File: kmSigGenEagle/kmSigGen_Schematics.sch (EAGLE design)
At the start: 36 parts, among them IC1 MEGA8-P

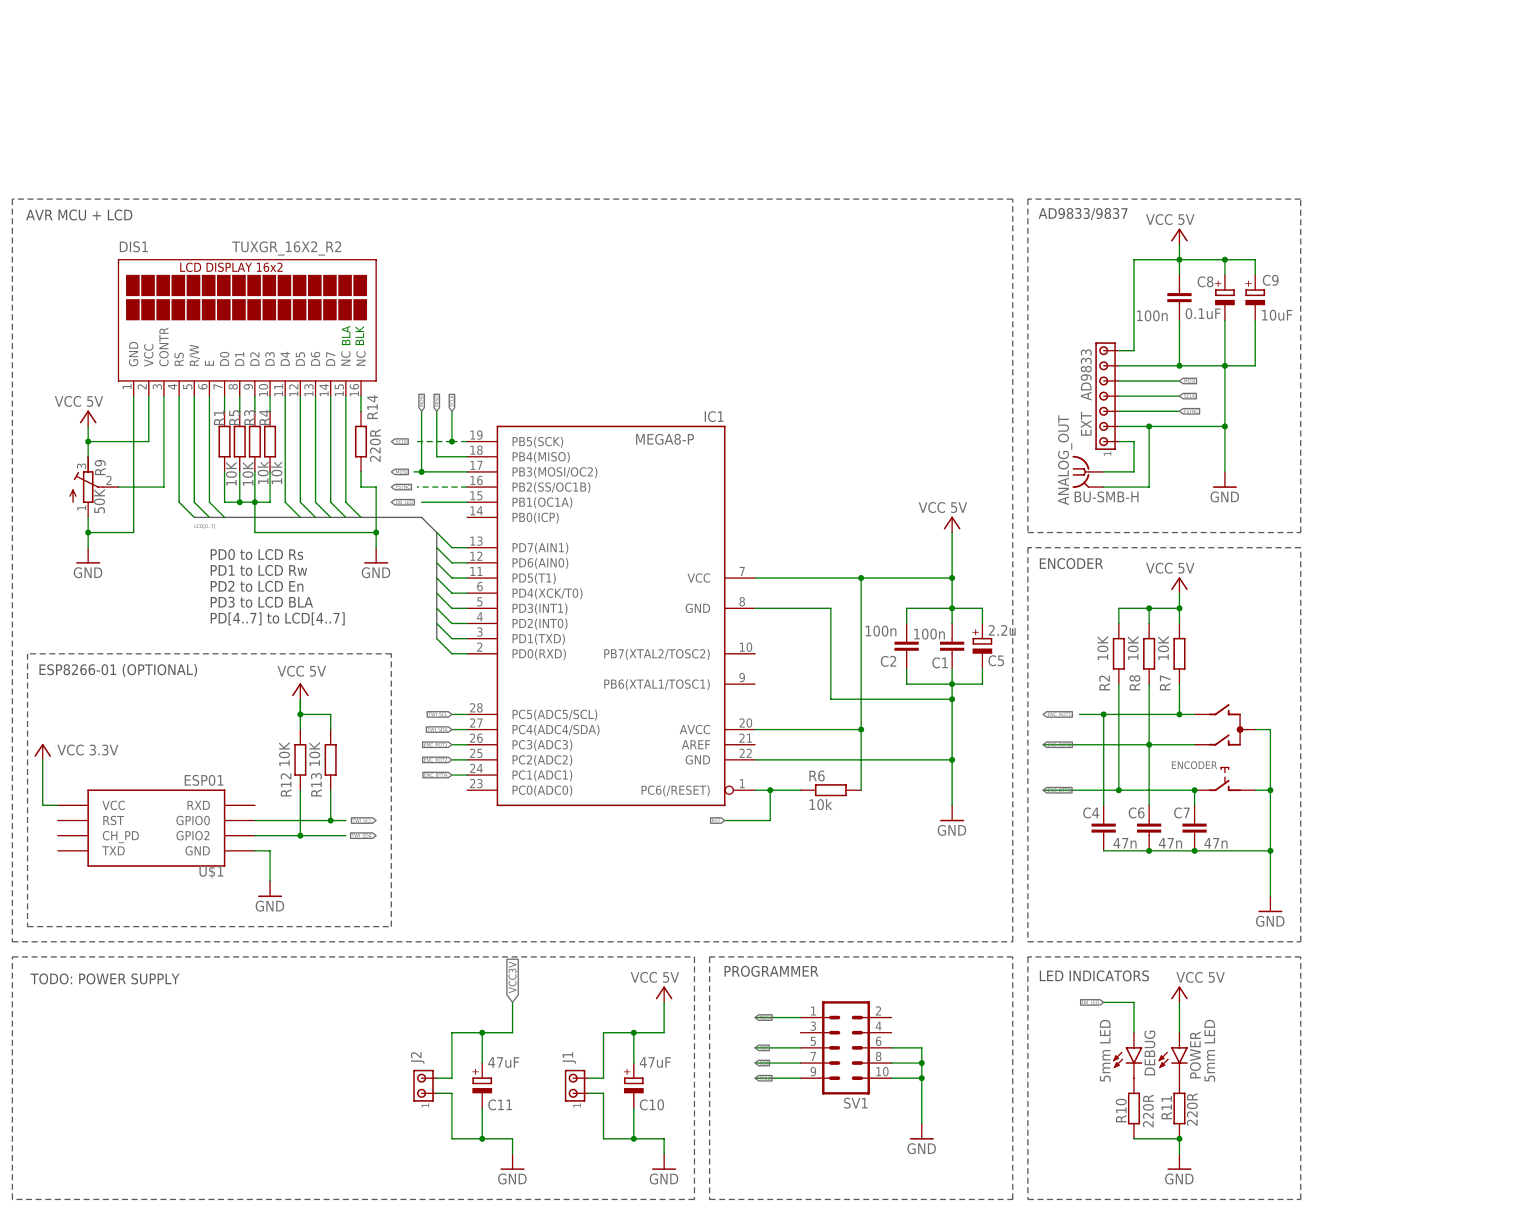
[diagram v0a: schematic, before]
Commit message: Updated schematics of encoder hardware
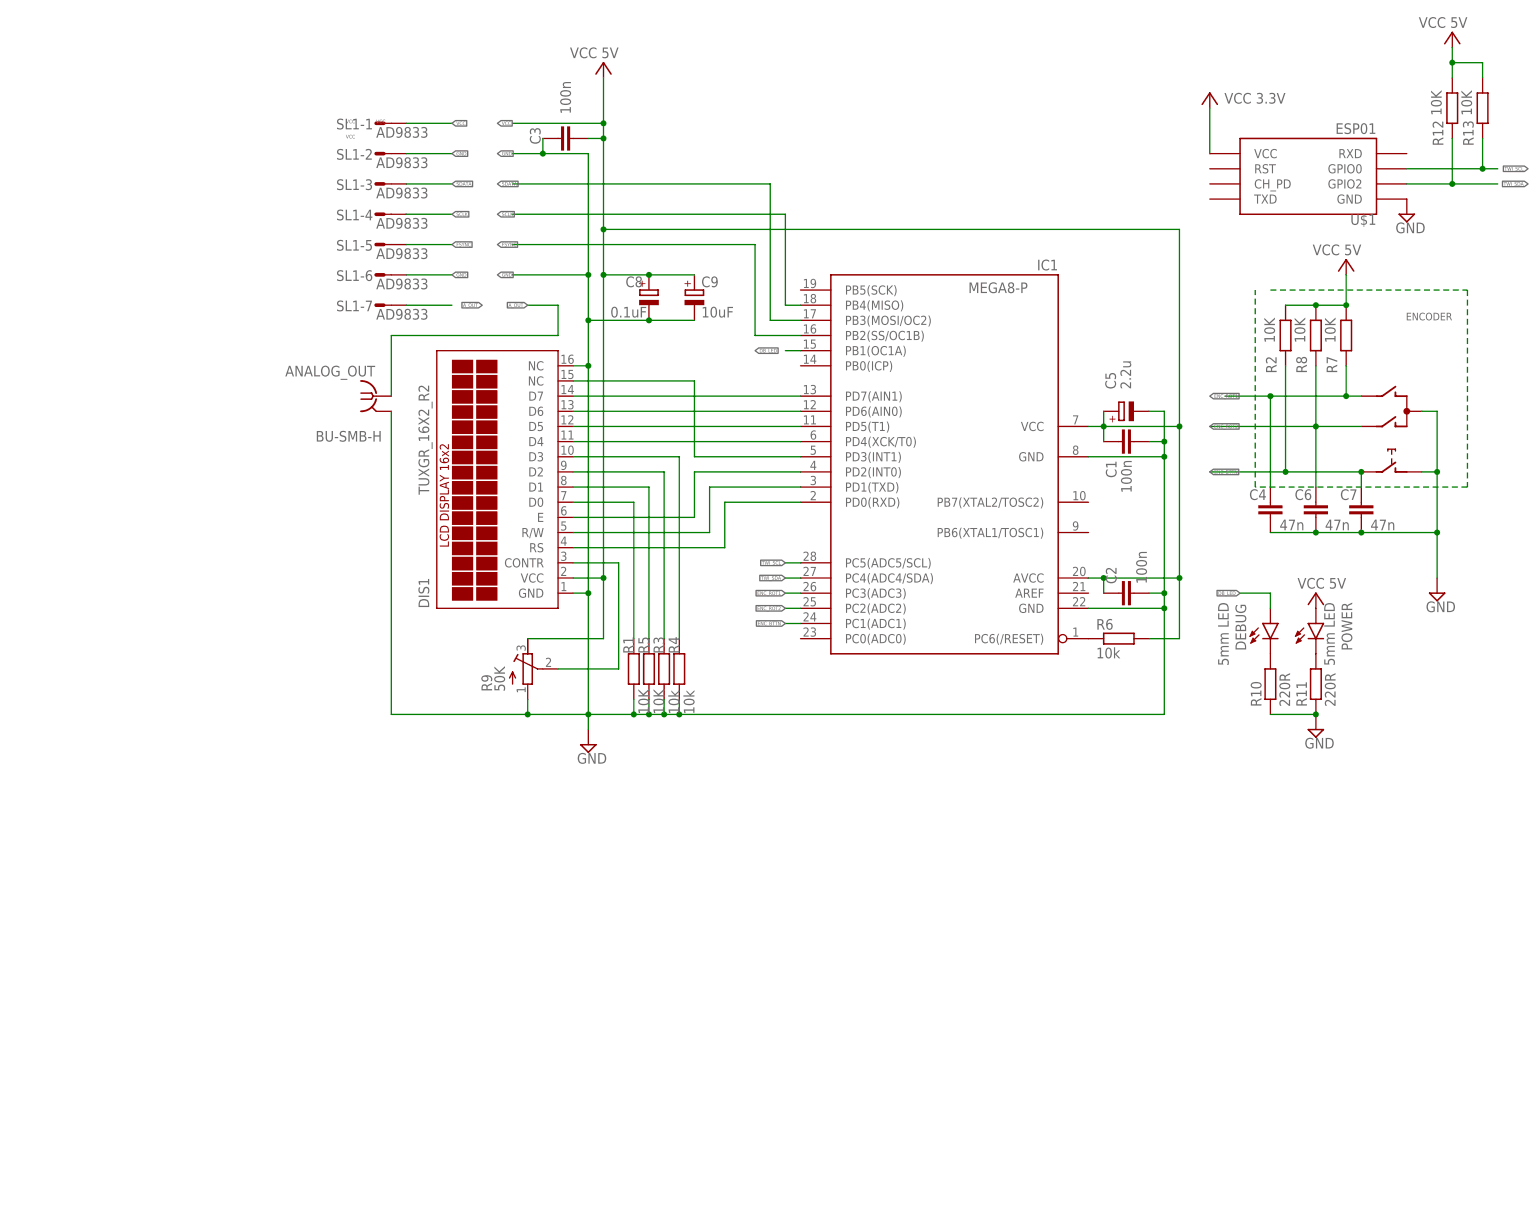
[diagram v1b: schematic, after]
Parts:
- removed C10, C11: 47uF, rcl:CPOL-EUB45181B
- removed EXT: AD9833, con-amp:MTA07-100
- removed J1, J2: (no value), con-amp:MTA02-156
- removed R14: 220R, rcl:R-EU_0207/10
- removed SV1: (no value), con-ml:ML10
- added SL1: AD9833, con-amp-quick:M07S
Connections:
- net LCD0 renamed N$7
- net LCD1 renamed N$8
- net LCD2 renamed N$9
- net LCD3 renamed N$6
- net LCD4 renamed N$5
- net LCD5 renamed N$4
- net LCD6 renamed N$3
- net LCD7 renamed LCD_D7
- removed net MISO: IC1.PB4(MISO), SV1.9
- removed net MOSI: EXT.5, IC1.PB3(MOSI/OC2), SV1.1
- removed net N$19: ANALOG_OUT.1, EXT.1
- removed net N$2: DIS1.NC@2, R14.2
- removed net RST: IC1.PC6(/RESET), R6.1, SV1.5
- removed net SCK: SV1.7
- removed net VCC3V: C11.+, J2.2, U$1.VCC
- new net A_OUT: ANALOG_OUT.1, SL1-7.S
- new net N$13: IC1.PC6(/RESET), R6.1
- new net SDATA: IC1.PB3(MOSI/OC2), SL1-3.S
- net FSYNC: now also SL1-5.S; no longer EXT.3
- net GND: now also C1.2, C2.2, DIS1.NC@2, SL1-2.S, SL1-6.S; no longer C1.1, C10.-, C11.-, C2.1, EXT.2, EXT.6, J1.1, J2.1, R14.1, SV1.10, SV1.6, SV1.8
- net SCLK: now also IC1.PB4(MISO), SL1-4.S; no longer EXT.4, IC1.PB5(SCK)
- net VCC: now also C1.1, C2.1, SL1-1.S, U$1.VCC; no longer C1.2, C10.+, C2.2, EXT.7, J1.2
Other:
- note removed: "AD9833/9837"
- note removed: "AVR MCU + LCD"
- note removed: "BLA"
- note removed: "BLK"
- note removed: "ENCODER"
- note removed: "ESP8266-01 (OPTIONAL)"
- note removed: "LED INDICATORS"
- note removed: "PD0 to LCD Rs PD1 to LCD Rw PD2 to LCD En PD3 to LCD BLA PD[4..7] to LCD[4..7]"
- note removed: "PROGRAMMER"
- note removed: "TODO: POWER SUPPLY"
- moved on the sheet: ANALOG_OUT, C1, C2, C4, C5, C6, C7, C8, C9, DEBUG, DIS1, ENCODER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

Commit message: Fixed issue with clearing wavetype after updating frequency from WiFi module; cleanup of Eagle Schematics, version changed to 1.0.1
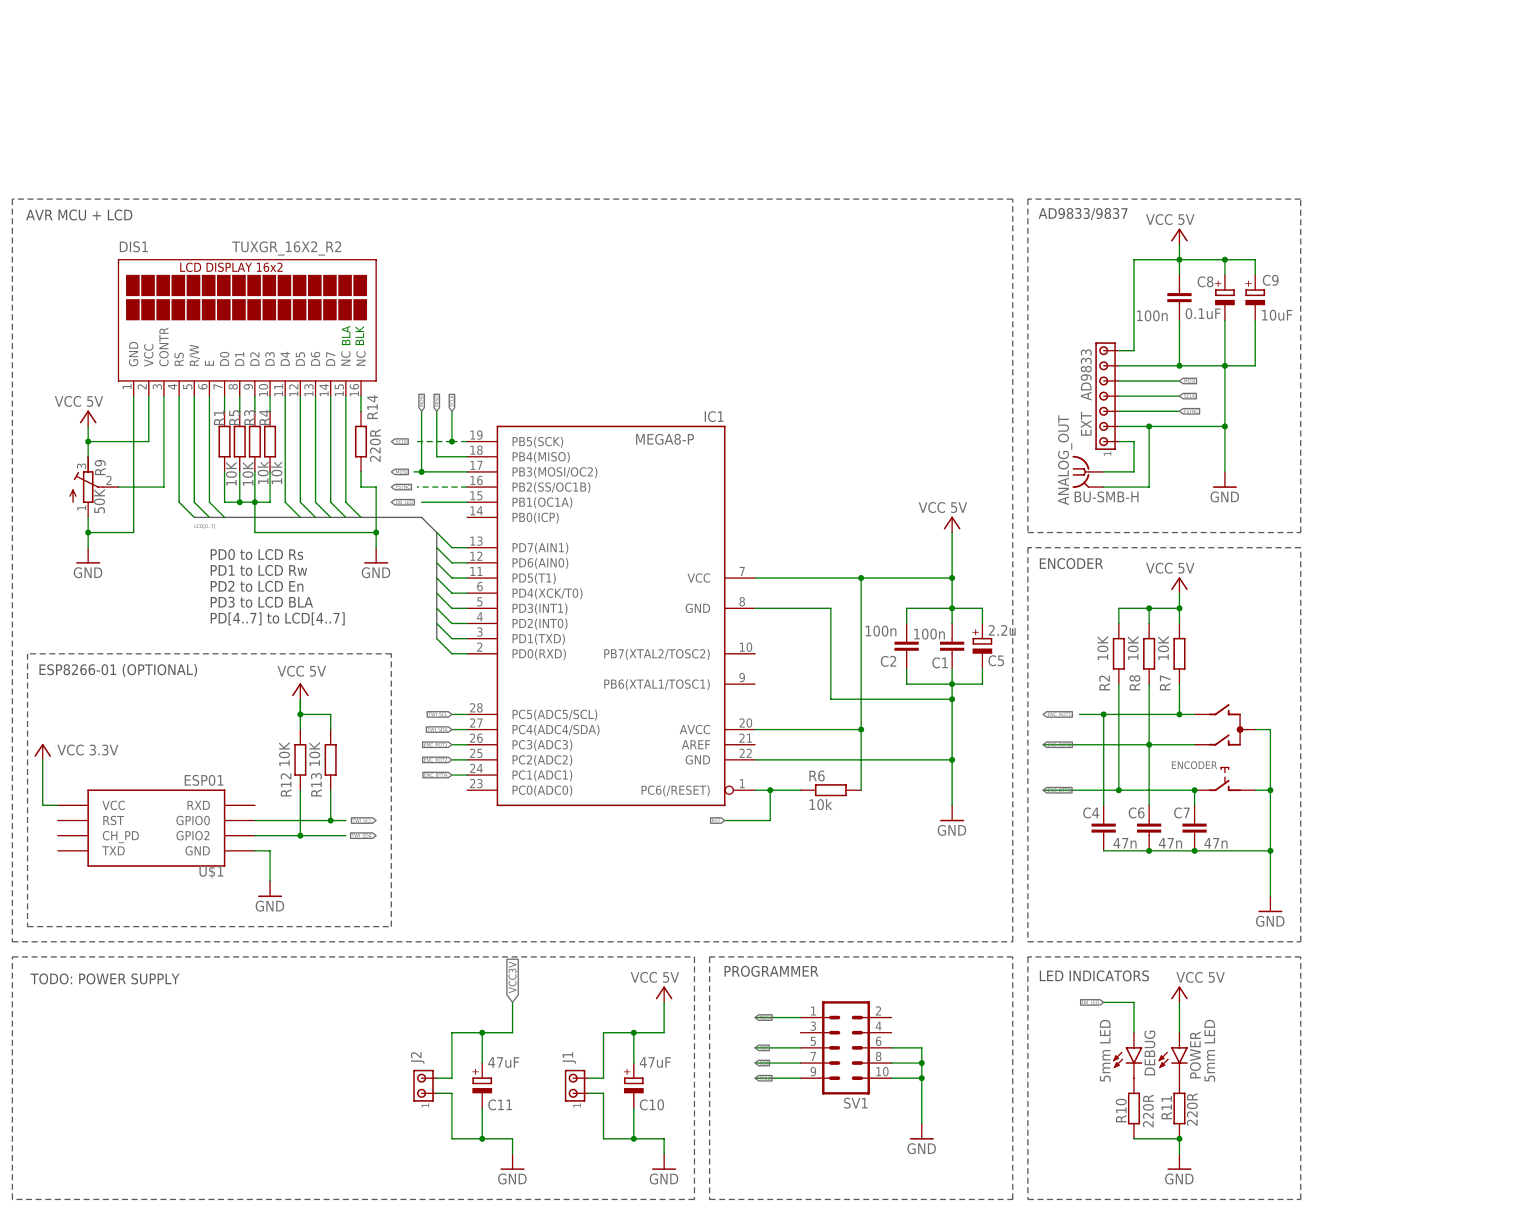
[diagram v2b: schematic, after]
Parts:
- removed SL1: AD9833, con-amp-quick:M07S
- added C10, C11: 47uF, rcl:CPOL-EUB45181B
- added EXT: AD9833, con-amp:MTA07-100
- added J1, J2: (no value), con-amp:MTA02-156
- added R14: 220R, rcl:R-EU_0207/10
- added SV1: (no value), con-ml:ML10
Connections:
- net LCD_D7 renamed LCD7
- net N$3 renamed LCD6
- net N$4 renamed LCD5
- net N$5 renamed LCD4
- net N$6 renamed LCD3
- net N$7 renamed LCD0
- net N$8 renamed LCD1
- net N$9 renamed LCD2
- removed net A_OUT: ANALOG_OUT.1, SL1-7.S
- removed net N$13: IC1.PC6(/RESET), R6.1
- removed net SDATA: IC1.PB3(MOSI/OC2), SL1-3.S
- new net MISO: IC1.PB4(MISO), SV1.9
- new net MOSI: EXT.5, IC1.PB3(MOSI/OC2), SV1.1
- new net N$19: ANALOG_OUT.1, EXT.1
- new net N$2: DIS1.NC@2, R14.2
- new net RST: IC1.PC6(/RESET), R6.1, SV1.5
- new net SCK: SV1.7
- new net VCC3V: C11.+, J2.2, U$1.VCC
- net FSYNC: now also EXT.3; no longer SL1-5.S
- net GND: now also C1.1, C10.-, C11.-, C2.1, EXT.2, EXT.6, J1.1, J2.1, R14.1, SV1.10, SV1.6, SV1.8; no longer C1.2, C2.2, DIS1.NC@2, SL1-2.S, SL1-6.S
- net SCLK: now also EXT.4, IC1.PB5(SCK); no longer IC1.PB4(MISO), SL1-4.S
- net VCC: now also C1.2, C10.+, C2.2, EXT.7, J1.2; no longer C1.1, C2.1, SL1-1.S, U$1.VCC
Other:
- note added: "AD9833/9837"
- note added: "AVR MCU + LCD"
- note added: "BLA"
- note added: "BLK"
- note added: "ENCODER"
- note added: "ESP8266-01 (OPTIONAL)"
- note added: "LED INDICATORS"
- note added: "PD0 to LCD Rs PD1 to LCD Rw PD2 to LCD En PD3 to LCD BLA PD[4..7] to LCD[4..7]"
- note added: "PROGRAMMER"
- note added: "TODO: POWER SUPPLY"
- moved on the sheet: ANALOG_OUT, C1, C2, C4, C5, C6, C7, C8, C9, DEBUG, DIS1, ENCODER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
